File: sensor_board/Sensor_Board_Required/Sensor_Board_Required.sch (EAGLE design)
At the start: 3 parts, among them J1 SL04, J2 SL03THROUGH_HOLE, J3 SL03THROUGH_HOLE

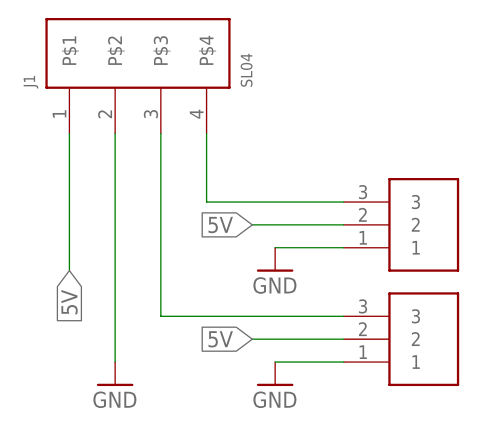
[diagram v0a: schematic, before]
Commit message: Rev1 to Sensor_Board_Required
Added tags for sensors.
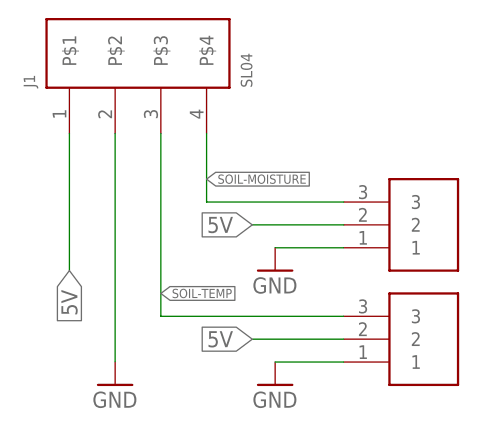
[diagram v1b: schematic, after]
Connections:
- net N$1 renamed SOIL-TEMP
- net N$2 renamed SOIL-MOISTURE
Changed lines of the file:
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@@
 </segment>
 </net>
-<net name="N$1" class="0">
+<net name="SOIL-TEMP" class="0">
 <segment>
 <pinref part="J3" gate="G$1" pin="3"/>
@@
 <wire x1="66.04" y1="50.8" x2="45.72" y2="50.8" width="0.1524" layer="91"/>
 <wire x1="45.72" y1="50.8" x2="45.72" y2="71.12" width="0.1524" layer="91"/>
+<label x="45.72" y="53.34" size="1.016" layer="95" xref="yes"/>
 </segment>
 </net>
-<net name="N$2" class="0">
+<net name="SOIL-MOISTURE" class="0">
 <segment>
 <pinref part="J2" gate="G$1" pin="3"/>
@@
 <wire x1="66.04" y1="63.5" x2="50.8" y2="63.5" width="0.1524" layer="91"/>
 <wire x1="50.8" y1="63.5" x2="50.8" y2="71.12" width="0.1524" layer="91"/>
+<label x="50.8" y="66.04" size="1.016" layer="95" xref="yes"/>
 </segment>
 </net>
